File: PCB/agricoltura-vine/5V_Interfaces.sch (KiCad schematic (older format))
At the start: 11 parts

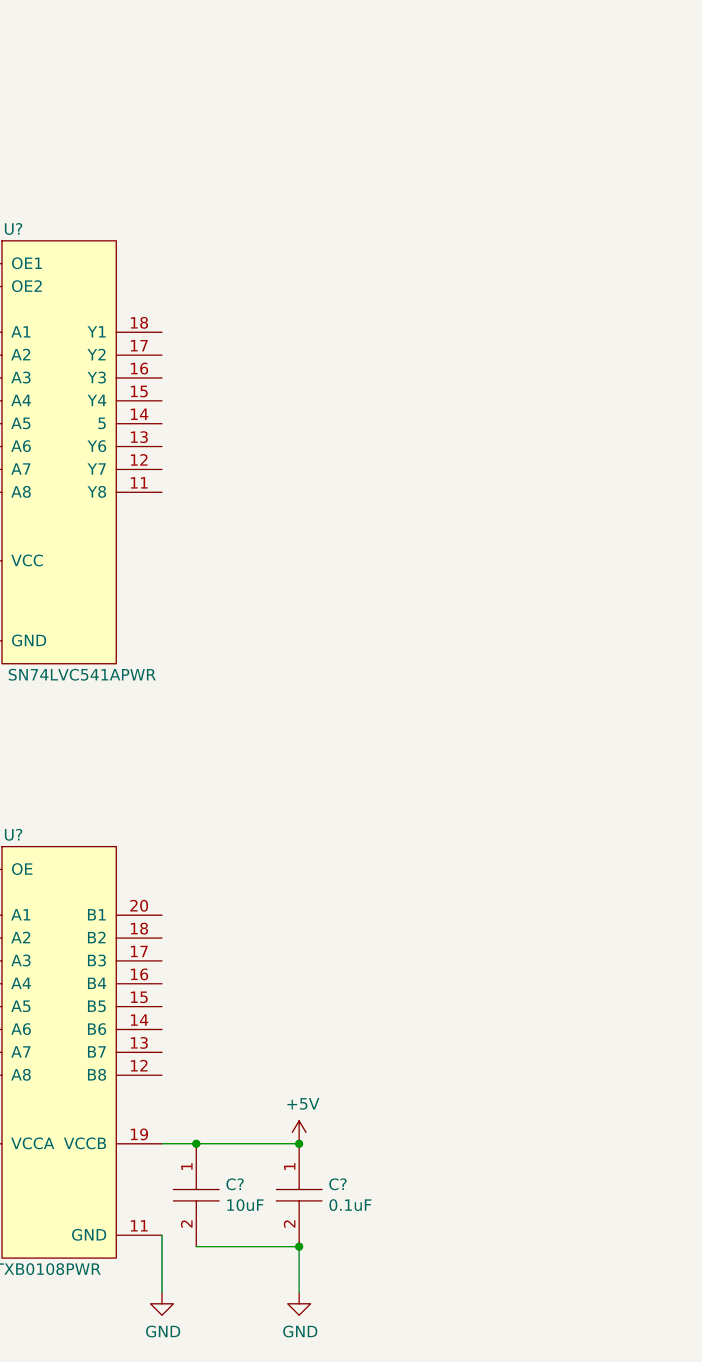
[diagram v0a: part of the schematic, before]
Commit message: Schematic Pass 1
All subsystem schematics are completed in their first pass, some features scaled back to make design more practical.
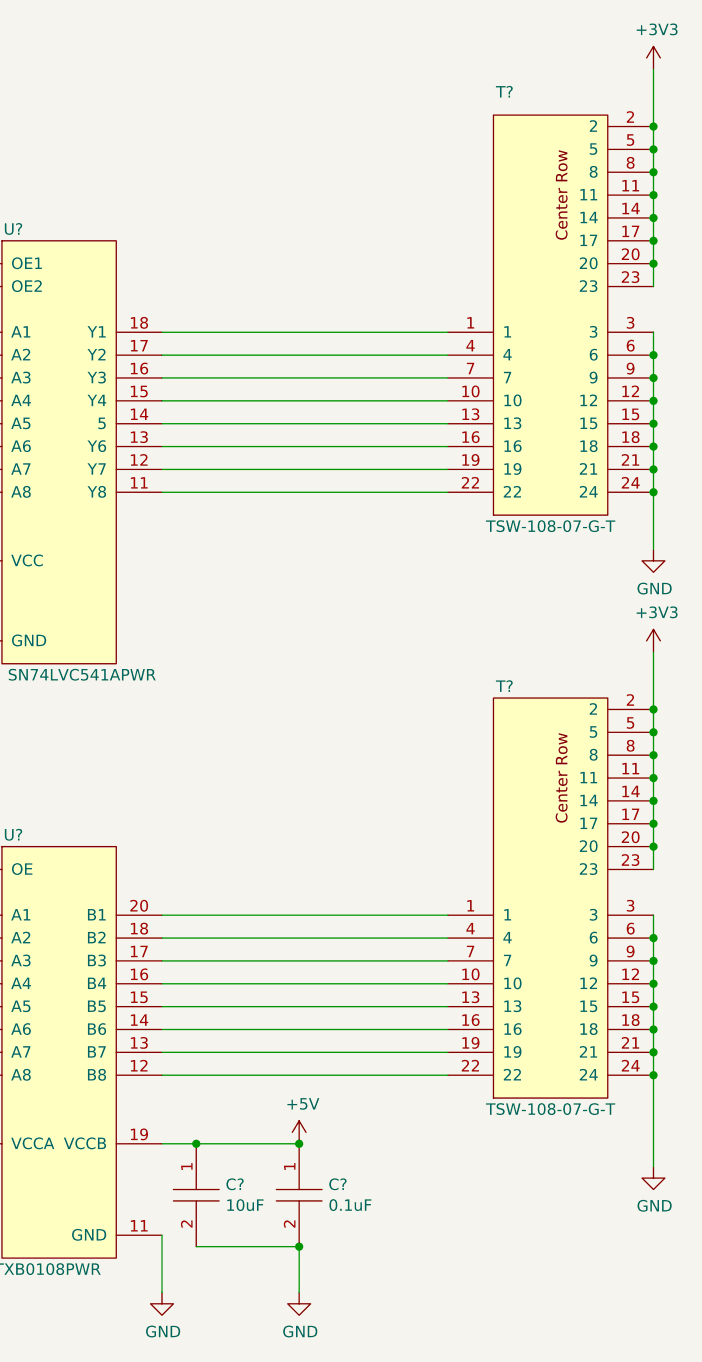
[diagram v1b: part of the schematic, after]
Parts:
- added T? (x2): TSW-108-07-G-T, AVR-KiCAD-Lib-Connectors:TSW-108-07-G-T, symbol AVR-KiCAD-Lib-Connectors:TSW-108-07-G-T
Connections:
- wire segments 22 -> 70
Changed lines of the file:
@@
 $EndComp
 Connection ~ 6800 5550
+$Comp
+L AVR-KiCAD-Lib-Connectors:TSW-108-07-G-T T?
+U 1 1 5F0EF8CA
+P 7650 2800
+F 0 "T?" H 7700 950 50  0000 C CNN
+F 1 "TSW-108-07-G-T" H 7900 2850 50  0000 C CNN
+F 2 "AVR-KiCAD-Lib-Connectors:TSW-108-07-G-T" H 7450 2800 50  0001 C CNN
+F 3 "http://suddendocs.samtec.com/catalog_english/tsw_th.pdf" H 7550 2900 50  0001 C CNN
+F 4 "2.51000" H 7750 3050 50  0001 C CNN "Cost QTY: 1"
+F 5 "1.39350" H 7850 3150 50  0001 C CNN "Cost QTY: 1000"
+F 6 "*" H 7950 3250 50  0001 C CNN "Cost QTY: 2500"
+F 7 "1.23557" H 8050 3350 50  0001 C CNN "Cost QTY: 5000"
+F 8 "1.20770" H 8150 3450 50  0001 C CNN "Cost QTY: 10000"
+F 9 "Samtec Inc." H 8250 3550 50  0001 C CNN "MFR"
+F 10 "TSW-108-07-G-T" H 8350 3650 50  0001 C CNN "MFR#"
+F 11 "Digikey" H 8450 3750 50  0001 C CNN "Vendor"
+F 12 "SAM10855-ND" H 8550 3850 50  0001 C CNN "Vendor #"
+F 13 "AVR" H 8650 3950 50  0001 C CNN "Designer"
+F 14 "10.92mm" H 8750 4050 50  0001 C CNN "Height"
+F 15 "6/18/2020" H 9850 5150 50  0001 C CNN "Date Created"
+F 16 "6/18/2020" H 8850 4150 50  0001 C CNN "Date Modified"
+F 17 "Yes" H 8950 4250 50  0001 C CNN "Lead-Free ?"
+F 18 "1" H 9050 4350 50  0001 C CNN "RoHS Levels"
+F 19 "SMT" H 9150 4450 50  0001 C CNN "Mounting"
+F 20 "24" H 9250 4550 50  0001 C CNN "Pin Count #"
+F 21 "Active" H 9350 4650 50  0001 C CNN "Status"
+F 22 "*" H 9450 4750 50  0001 C CNN "Tolerance"
+F 23 "Connector" H 9550 4850 50  0001 C CNN "Type"
+F 24 "*" H 9650 4950 50  0001 C CNN "Voltage"
+F 25 "*" H 9750 5100 50  0001 C CNN "Package"
+F 26 "Connector Header Through Hole 24 position 0.100\" (2.54mm)" H 10150 5500 50  0001 C CNN "Description"
+F 27 "3X08" H 9950 5300 50  0001 C CNN "_Value_"
+F 28 "*" H 10050 5400 50  0001 C CNN "Management_ID"
+	1    7650 2800
+	1    0    0    1
+$EndComp
+$Comp
+L AVR-KiCAD-Lib-Connectors:TSW-108-07-G-T T?
+U 1 1 5F0F4F0C
+P 7650 5350
+F 0 "T?" H 7700 3550 50  0000 C CNN
+F 1 "TSW-108-07-G-T" H 7900 5400 50  0000 C CNN
+F 2 "AVR-KiCAD-Lib-Connectors:TSW-108-07-G-T" H 7450 5350 50  0001 C CNN
+F 3 "http://suddendocs.samtec.com/catalog_english/tsw_th.pdf" H 7550 5450 50  0001 C CNN
+F 4 "2.51000" H 7750 5600 50  0001 C CNN "Cost QTY: 1"
+F 5 "1.39350" H 7850 5700 50  0001 C CNN "Cost QTY: 1000"
+F 6 "*" H 7950 5800 50  0001 C CNN "Cost QTY: 2500"
+F 7 "1.23557" H 8050 5900 50  0001 C CNN "Cost QTY: 5000"
+F 8 "1.20770" H 8150 6000 50  0001 C CNN "Cost QTY: 10000"
+F 9 "Samtec Inc." H 8250 6100 50  0001 C CNN "MFR"
+F 10 "TSW-108-07-G-T" H 8350 6200 50  0001 C CNN "MFR#"
+F 11 "Digikey" H 8450 6300 50  0001 C CNN "Vendor"
+F 12 "SAM10855-ND" H 8550 6400 50  0001 C CNN "Vendor #"
+F 13 "AVR" H 8650 6500 50  0001 C CNN "Designer"
+F 14 "10.92mm" H 8750 6600 50  0001 C CNN "Height"
+F 15 "6/18/2020" H 9850 7700 50  0001 C CNN "Date Created"
+F 16 "6/18/2020" H 8850 6700 50  0001 C CNN "Date Modified"
+F 17 "Yes" H 8950 6800 50  0001 C CNN "Lead-Free ?"
+F 18 "1" H 9050 6900 50  0001 C CNN "RoHS Levels"
+F 19 "SMT" H 9150 7000 50  0001 C CNN "Mounting"
+F 20 "24" H 9250 7100 50  0001 C CNN "Pin Count #"
+F 21 "Active" H 9350 7200 50  0001 C CNN "Status"
+F 22 "*" H 9450 7300 50  0001 C CNN "Tolerance"
+F 23 "Connector" H 9550 7400 50  0001 C CNN "Type"
+F 24 "*" H 9650 7500 50  0001 C CNN "Voltage"
+F 25 "*" H 9750 7650 50  0001 C CNN "Package"
+F 26 "Connector Header Through Hole 24 position 0.100\" (2.54mm)" H 10150 8050 50  0001 C CNN "Description"
+F 27 "3X08" H 9950 7850 50  0001 C CNN "_Value_"
+F 28 "*" H 10050 7950 50  0001 C CNN "Management_ID"
+	1    7650 5350
+	1    0    0    1
+$EndComp
+Wire Wire Line
+	6200 4550 7450 4550
+Wire Wire Line
+	7450 4650 6200 4650
+Wire Wire Line
+	6200 4750 7450 4750
+Wire Wire Line
+	7450 4850 6200 4850
+Wire Wire Line
+	7450 5050 6200 5050
+Wire Wire Line
+	6200 4950 7450 4950
+Wire Wire Line
+	6200 5150 7450 5150
+Wire Wire Line
+	6200 5250 7450 5250
+Wire Wire Line
+	6200 2000 7450 2000
+Wire Wire Line
+	7450 2100 6200 2100
+Wire Wire Line
+	6200 2200 7450 2200
+Wire Wire Line
+	7450 2300 6200 2300
+Wire Wire Line
+	7450 2500 6200 2500
+Wire Wire Line
+	6200 2400 7450 2400
+Wire Wire Line
+	6200 2600 7450 2600
+Wire Wire Line
+	6200 2700 7450 2700
+$Comp
+L power:GND #PWR?
+U 1 1 5F0FCCF6
+P 8350 2950
+F 0 "#PWR?" H 8350 2700 50  0001 C CNN
+F 1 "GND" H 8355 2777 50  0000 C CNN
+F 2 "" H 8350 2950 50  0001 C CNN
+F 3 "" H 8350 2950 50  0001 C CNN
+	1    8350 2950
+	1    0    0    -1
+$EndComp
+$Comp
+L power:GND #PWR?
+U 1 1 5F0FD1DB
+P 8350 5650
+F 0 "#PWR?" H 8350 5400 50  0001 C CNN
+F 1 "GND" H 8355 5477 50  0000 C CNN
+F 2 "" H 8350 5650 50  0001 C CNN
+F 3 "" H 8350 5650 50  0001 C CNN
+	1    8350 5650
+	1    0    0    -1
+$EndComp
+Wire Wire Line
+	8350 4550 8350 4650
+Connection ~ 8350 4650
+Wire Wire Line
+	8350 4650 8350 4750
+Connection ~ 8350 4750
+Wire Wire Line
+	8350 4750 8350 4850
+Connection ~ 8350 4850
+Wire Wire Line
+	8350 4850 8350 4950
+Connection ~ 8350 4950
+Wire Wire Line
+	8350 4950 8350 5050
+Connection ~ 8350 5050
+Wire Wire Line
+	8350 5050 8350 5150
+Connection ~ 8350 5150
+Wire Wire Line
+	8350 5150 8350 5250
+Connection ~ 8350 5250
+Wire Wire Line
+	8350 5250 8350 5650
+Wire Wire Line
+	8350 2950 8350 2700
+Connection ~ 8350 2100
+Wire Wire Line
+	8350 2100 8350 2000
+Connection ~ 8350 2200
+Wire Wire Line
+	8350 2200 8350 2100
+Connection ~ 8350 2300
+Wire Wire Line
+	8350 2300 8350 2200
+Connection ~ 8350 2400
+Wire Wire Line
+	8350 2400 8350 2300
+Connection ~ 8350 2500
+Wire Wire Line
+	8350 2500 8350 2400
+Connection ~ 8350 2600
+Wire Wire Line
+	8350 2600 8350 2500
+Connection ~ 8350 2700
+Wire Wire Line
+	8350 2700 8350 2600
+$Comp
+L power:+3V3 #PWR?
+U 1 1 5F0FF4C1
+P 8350 850
+F 0 "#PWR?" H 8350 700 50  0001 C CNN
+F 1 "+3V3" H 8365 1023 50  0000 C CNN
+F 2 "" H 8350 850 50  0001 C CNN
+F 3 "" H 8350 850 50  0001 C CNN
+	1    8350 850
+	1    0    0    -1
+$EndComp
+Wire Wire Line
+	8350 850  8350 1100
+Connection ~ 8350 1100
+Wire Wire Line
+	8350 1100 8350 1200
+Connection ~ 8350 1200
+Wire Wire Line
+	8350 1200 8350 1300
+Connection ~ 8350 1300
+Wire Wire Line
+	8350 1300 8350 1400
+Connection ~ 8350 1400
+Wire Wire Line
+	8350 1400 8350 1500
+Connection ~ 8350 1500
+Wire Wire Line
+	8350 1500 8350 1600
+Connection ~ 8350 1600
+Wire Wire Line
+	8350 1600 8350 1700
+Connection ~ 8350 1700
+Wire Wire Line
+	8350 1700 8350 1800
+$Comp
+L power:+3V3 #PWR?
+U 1 1 5F101EF5
+P 8350 3400
+F 0 "#PWR?" H 8350 3250 50  0001 C CNN
+F 1 "+3V3" H 8365 3573 50  0000 C CNN
+F 2 "" H 8350 3400 50  0001 C CNN
+F 3 "" H 8350 3400 50  0001 C CNN
+	1    8350 3400
+	1    0    0    -1
+$EndComp
+Wire Wire Line
+	8350 3400 8350 3650
+Connection ~ 8350 3650
+Wire Wire Line
+	8350 3650 8350 3750
+Connection ~ 8350 3750
+Wire Wire Line
+	8350 3750 8350 3850
+Connection ~ 8350 3850
+Wire Wire Line
+	8350 3850 8350 3950
+Connection ~ 8350 3950
+Wire Wire Line
+	8350 3950 8350 4050
+Connection ~ 8350 4050
+Wire Wire Line
+	8350 4050 8350 4150
+Connection ~ 8350 4150
+Wire Wire Line
+	8350 4150 8350 4250
+Connection ~ 8350 4250
+Wire Wire Line
+	8350 4250 8350 4350
 $EndSCHEMATC

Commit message: Board
Board shape defined, though subject to change. Schematic anotated and parts exported to board.
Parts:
- gave numbers to parts that had none: 13
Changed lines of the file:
@@
 $EndDescr
 $Comp
-L AVR-KiCAD-Lib-ICs:SN74LV541APWR U?
+L AVR-KiCAD-Lib-ICs:SN74LV541APWR U8
 U 1 1 5EF9CCA5
 P 5500 1600
-F 0 "U?" H 5550 1650 50  0000 C CNN
+F 0 "U8" H 5550 1650 50  0000 C CNN
 F 1 "SN74LV541APWR" H 5550 1700 50  0001 C CNN
 F 2 "AVR-KiCAD-Lib-ICs:SN74LVC541APWR" H 5300 1500 50  0001 C CNN
@@
 $EndComp
 $Comp
-L AVR-KiCAD-Lib-ICs:TXB0108PWR U?
+L AVR-KiCAD-Lib-ICs:TXB0108PWR U9
 U 1 1 5EFA6366
 P 5500 4250
-F 0 "U?" H 5550 4300 50  0000 C CNN
+F 0 "U9" H 5550 4300 50  0000 C CNN
 F 1 "TXB0108PWR" H 5200 4650 50  0001 C CNN
 F 2 "AVR-KiCAD-Lib-ICs:TXB0108PWR" H 4850 4850 50  0001 C CNN
@@
 P 5100 1400
 AR Path="/5EE8264D/5EFB2B69" Ref="R?"  Part="1"
-AR Path="/5EF943A9/5EFB2B69" Ref="R?"  Part="1"
-F 0 "R?" V 5050 1450 50  0000 L CNN
+AR Path="/5EF943A9/5EFB2B69" Ref="R21"  Part="1"
+F 0 "R21" V 5050 1450 50  0000 L CNN
 F 1 "RC0402FR-071KL" V 5100 1488 50  0001 L CNN
 F 2 "AVR-KiCAD-Lib-Resistors:R0402" H 5100 1400 50  0001 C CNN
@@
 P 4850 1400
 AR Path="/5EE8264D/5EFB5F9C" Ref="R?"  Part="1"
-AR Path="/5EF943A9/5EFB5F9C" Ref="R?"  Part="1"
-F 0 "R?" V 4800 1450 50  0000 L CNN
+AR Path="/5EF943A9/5EFB5F9C" Ref="R20"  Part="1"
+F 0 "R20" V 4800 1450 50  0000 L CNN
 F 1 "RC0402FR-071KL" V 4850 1488 50  0001 L CNN
 F 2 "AVR-KiCAD-Lib-Resistors:R0402" H 4850 1400 50  0001 C CNN
@@
 	4850 1200 5100 1200
 $Comp
-L power:+3V3 #PWR?
+L power:+3V3 #PWR054
 U 1 1 5EFB81F8
 P 4850 1200
-F 0 "#PWR?" H 4850 1050 50  0001 C CNN
+F 0 "#PWR054" H 4850 1050 50  0001 C CNN
 F 1 "+3V3" H 4865 1373 50  0000 C CNN
 F 2 "" H 4850 1200 50  0001 C CNN
@@
 P 5100 4150
 AR Path="/5EE8264D/5EFB87DA" Ref="R?"  Part="1"
-AR Path="/5EF943A9/5EFB87DA" Ref="R?"  Part="1"
-F 0 "R?" V 5050 4200 50  0000 L CNN
+AR Path="/5EF943A9/5EFB87DA" Ref="R22"  Part="1"
+F 0 "R22" V 5050 4200 50  0000 L CNN
 F 1 "RC0402FR-071KL" V 5100 4238 50  0001 L CNN
 F 2 "AVR-KiCAD-Lib-Resistors:R0402" H 5100 4150 50  0001 C CNN
@@
 $EndComp
 $Comp
-L power:+3V3 #PWR?
+L power:+3V3 #PWR055
 U 1 1 5EFBB16E
 P 5100 3950
-F 0 "#PWR?" H 5100 3800 50  0001 C CNN
+F 0 "#PWR055" H 5100 3800 50  0001 C CNN
 F 1 "+3V3" H 5115 4123 50  0000 C CNN
 F 2 "" H 5100 3950 50  0001 C CNN
@@
 AR Path="/5EE82896/5EFC2554" Ref="C?"  Part="1"
 AR Path="/5EE82702/5EFC2554" Ref="C?"  Part="1"
-AR Path="/5EF943A9/5EFC2554" Ref="C?"  Part="1"
-F 0 "C?" V 4229 3328 50  0000 L CNN
+AR Path="/5EF943A9/5EFC2554" Ref="C33"  Part="1"
+F 0 "C33" V 4229 3328 50  0000 L CNN
 F 1 "C0402C104K9PACTU" H 4300 3400 50  0001 C CNN
 F 2 "AVR-KiCAD-Lib-Resistors:R0402" H 4050 3200 50  0001 C CNN
@@
 AR Path="/5EE82896/5EFC2573" Ref="C?"  Part="1"
 AR Path="/5EE82702/5EFC2573" Ref="C?"  Part="1"
-AR Path="/5EF943A9/5EFC2573" Ref="C?"  Part="1"
-F 0 "C?" V 4729 3328 50  0000 L CNN
+AR Path="/5EF943A9/5EFC2573" Ref="C35"  Part="1"
+F 0 "C35" V 4729 3328 50  0000 L CNN
 F 1 "GRM188R61A106KE69J" H 4800 3400 50  0001 C CNN
 F 2 "AVR-KiCAD-Lib-Capacitors:C0603" H 4550 3200 50  0001 C CNN
@@
 $EndComp
 $Comp
-L power:GND #PWR?
+L power:GND #PWR056
 U 1 1 5EFC274D
 P 5300 3350
-F 0 "#PWR?" H 5300 3100 50  0001 C CNN
+F 0 "#PWR056" H 5300 3100 50  0001 C CNN
 F 1 "GND" H 5305 3177 50  0000 C CNN
 F 2 "" H 5300 3350 50  0001 C CNN
@@
 $EndComp
 $Comp
-L power:GND #PWR?
+L power:GND #PWR051
 U 1 1 5EFC333F
 P 4500 3450
-F 0 "#PWR?" H 4500 3200 50  0001 C CNN
+F 0 "#PWR051" H 4500 3200 50  0001 C CNN
 F 1 "GND" H 4505 3277 50  0000 C CNN
 F 2 "" H 4500 3450 50  0001 C CNN
@@
 	4750 3000 4250 3000
 $Comp
-L power:+3V3 #PWR?
+L power:+3V3 #PWR050
 U 1 1 5EFC3DF1
 P 4250 3000
-F 0 "#PWR?" H 4250 2850 50  0001 C CNN
+F 0 "#PWR050" H 4250 2850 50  0001 C CNN
 F 1 "+3V3" H 4265 3173 50  0000 C CNN
 F 2 "" H 4250 3000 50  0001 C CNN
@@
 Connection ~ 4250 3000
 $Comp
-L power:GND #PWR?
+L power:GND #PWR057
 U 1 1 5EFCC144
 P 6200 6200
-F 0 "#PWR?" H 6200 5950 50  0001 C CNN
+F 0 "#PWR057" H 6200 5950 50  0001 C CNN
 F 1 "GND" H 6205 6027 50  0000 C CNN
 F 2 "" H 6200 6200 50  0001 C CNN
@@
 AR Path="/5EE82896/5EFD0CC7" Ref="C?"  Part="1"
 AR Path="/5EE82702/5EFD0CC7" Ref="C?"  Part="1"
-AR Path="/5EF943A9/5EFD0CC7" Ref="C?"  Part="1"
-F 0 "C?" V 4629 5878 50  0000 L CNN
+AR Path="/5EF943A9/5EFD0CC7" Ref="C34"  Part="1"
+F 0 "C34" V 4629 5878 50  0000 L CNN
 F 1 "C0402C104K9PACTU" H 4700 5950 50  0001 C CNN
 F 2 "AVR-KiCAD-Lib-Resistors:R0402" H 4450 5750 50  0001 C CNN
@@
 AR Path="/5EE82896/5EFD0CE6" Ref="C?"  Part="1"
 AR Path="/5EE82702/5EFD0CE6" Ref="C?"  Part="1"
-AR Path="/5EF943A9/5EFD0CE6" Ref="C?"  Part="1"
-F 0 "C?" V 5129 5878 50  0000 L CNN
+AR Path="/5EF943A9/5EFD0CE6" Ref="C36"  Part="1"
+F 0 "C36" V 5129 5878 50  0000 L CNN
 F 1 "GRM188R61A106KE69J" H 5200 5950 50  0001 C CNN
 F 2 "AVR-KiCAD-Lib-Capacitors:C0603" H 4950 5750 50  0001 C CNN
@@
 AR Path="/5EE82896/5EFD6E81" Ref="C?"  Part="1"
 AR Path="/5EE82702/5EFD6E81" Ref="C?"  Part="1"
-AR Path="/5EF943A9/5EFD6E81" Ref="C?"  Part="1"
-F 0 "C?" V 6779 5878 50  0000 L CNN
+AR Path="/5EF943A9/5EFD6E81" Ref="C38"  Part="1"
+F 0 "C38" V 6779 5878 50  0000 L CNN
 F 1 "C0402C104K9PACTU" H 6850 5950 50  0001 C CNN
 F 2 "AVR-KiCAD-Lib-Resistors:R0402" H 6600 5750 50  0001 C CNN
@@
 AR Path="/5EE82896/5EFD6EA0" Ref="C?"  Part="1"
 AR Path="/5EE82702/5EFD6EA0" Ref="C?"  Part="1"
-AR Path="/5EF943A9/5EFD6EA0" Ref="C?"  Part="1"
-F 0 "C?" V 6329 5878 50  0000 L CNN
+AR Path="/5EF943A9/5EFD6EA0" Ref="C37"  Part="1"
+F 0 "C37" V 6329 5878 50  0000 L CNN
 F 1 "GRM188R61A106KE69J" H 6400 5950 50  0001 C CNN
 F 2 "AVR-KiCAD-Lib-Capacitors:C0603" H 6150 5750 50  0001 C CNN
@@
 	6200 6200 6200 5950
 $Comp
-L power:GND #PWR?
+L power:GND #PWR059
 U 1 1 5EFDD1F1
 P 6800 6200
-F 0 "#PWR?" H 6800 5950 50  0001 C CNN
+F 0 "#PWR059" H 6800 5950 50  0001 C CNN
 F 1 "GND" H 6805 6027 50  0000 C CNN
 F 2 "" H 6800 6200 50  0001 C CNN
@@
 Connection ~ 6800 6000
 $Comp
-L power:GND #PWR?
+L power:GND #PWR053
 U 1 1 5EFDD89F
 P 4650 6200
-F 0 "#PWR?" H 4650 5950 50  0001 C CNN
+F 0 "#PWR053" H 4650 5950 50  0001 C CNN
 F 1 "GND" H 4655 6027 50  0000 C CNN
 F 2 "" H 4650 6200 50  0001 C CNN
@@
 	5150 5550 4650 5550
 $Comp
-L power:+3V3 #PWR?
+L power:+3V3 #PWR052
 U 1 1 5EFDE5C9
 P 4650 5550
-F 0 "#PWR?" H 4650 5400 50  0001 C CNN
+F 0 "#PWR052" H 4650 5400 50  0001 C CNN
 F 1 "+3V3" H 4665 5723 50  0000 C CNN
 F 2 "" H 4650 5550 50  0001 C CNN
@@
 Connection ~ 4650 5550
 $Comp
-L power:+5V #PWR?
+L power:+5V #PWR058
 U 1 1 5EFDED10
 P 6800 5550
-F 0 "#PWR?" H 6800 5400 50  0001 C CNN
+F 0 "#PWR058" H 6800 5400 50  0001 C CNN
 F 1 "+5V" H 6815 5723 50  0000 C CNN
 F 2 "" H 6800 5550 50  0001 C CNN
@@
 Connection ~ 6800 5550
 $Comp
-L AVR-KiCAD-Lib-Connectors:TSW-108-07-G-T T?
+L AVR-KiCAD-Lib-Connectors:TSW-108-07-G-T T19
 U 1 1 5F0EF8CA
 P 7650 2800
-F 0 "T?" H 7700 950 50  0000 C CNN
+F 0 "T19" H 7700 950 50  0000 C CNN
 F 1 "TSW-108-07-G-T" H 7900 2850 50  0000 C CNN
 F 2 "AVR-KiCAD-Lib-Connectors:TSW-108-07-G-T" H 7450 2800 50  0001 C CNN
@@
 $EndComp
 $Comp
-L AVR-KiCAD-Lib-Connectors:TSW-108-07-G-T T?
+L AVR-KiCAD-Lib-Connectors:TSW-108-07-G-T T20
 U 1 1 5F0F4F0C
 P 7650 5350
-F 0 "T?" H 7700 3550 50  0000 C CNN
+F 0 "T20" H 7700 3550 50  0000 C CNN
 F 1 "TSW-108-07-G-T" H 7900 5400 50  0000 C CNN
 F 2 "AVR-KiCAD-Lib-Connectors:TSW-108-07-G-T" H 7450 5350 50  0001 C CNN
@@
 	6200 2700 7450 2700
 $Comp
-L power:GND #PWR?
+L power:GND #PWR061
 U 1 1 5F0FCCF6
 P 8350 2950
-F 0 "#PWR?" H 8350 2700 50  0001 C CNN
+F 0 "#PWR061" H 8350 2700 50  0001 C CNN
 F 1 "GND" H 8355 2777 50  0000 C CNN
 F 2 "" H 8350 2950 50  0001 C CNN
@@
 $EndComp
 $Comp
-L power:GND #PWR?
+L power:GND #PWR063
 U 1 1 5F0FD1DB
 P 8350 5650
-F 0 "#PWR?" H 8350 5400 50  0001 C CNN
+F 0 "#PWR063" H 8350 5400 50  0001 C CNN
 F 1 "GND" H 8355 5477 50  0000 C CNN
 F 2 "" H 8350 5650 50  0001 C CNN
@@
 	8350 2700 8350 2600
 $Comp
-L power:+3V3 #PWR?
+L power:+3V3 #PWR060
 U 1 1 5F0FF4C1
 P 8350 850
-F 0 "#PWR?" H 8350 700 50  0001 C CNN
+F 0 "#PWR060" H 8350 700 50  0001 C CNN
 F 1 "+3V3" H 8365 1023 50  0000 C CNN
 F 2 "" H 8350 850 50  0001 C CNN
@@
 	8350 1700 8350 1800
 $Comp
-L power:+3V3 #PWR?
+L power:+3V3 #PWR062
 U 1 1 5F101EF5
 P 8350 3400
-F 0 "#PWR?" H 8350 3250 50  0001 C CNN
+F 0 "#PWR062" H 8350 3250 50  0001 C CNN
 F 1 "+3V3" H 8365 3573 50  0000 C CNN
 F 2 "" H 8350 3400 50  0001 C CNN
